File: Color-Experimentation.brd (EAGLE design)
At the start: 40.6 x 69.5 mm, 26 parts, among them J1 10118193-0001LF, U2 ATTINY85-20MUR

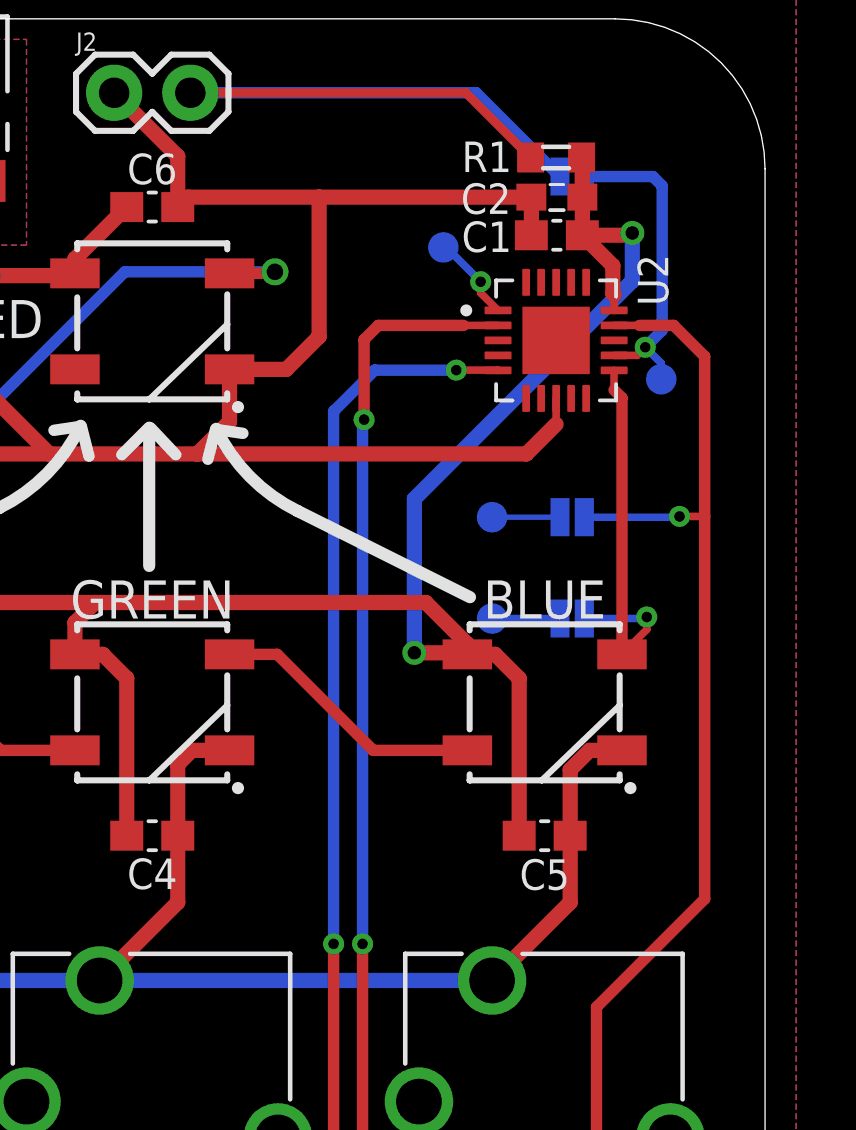
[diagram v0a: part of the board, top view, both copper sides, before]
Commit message: Switch microcontroller for availability: v1.1
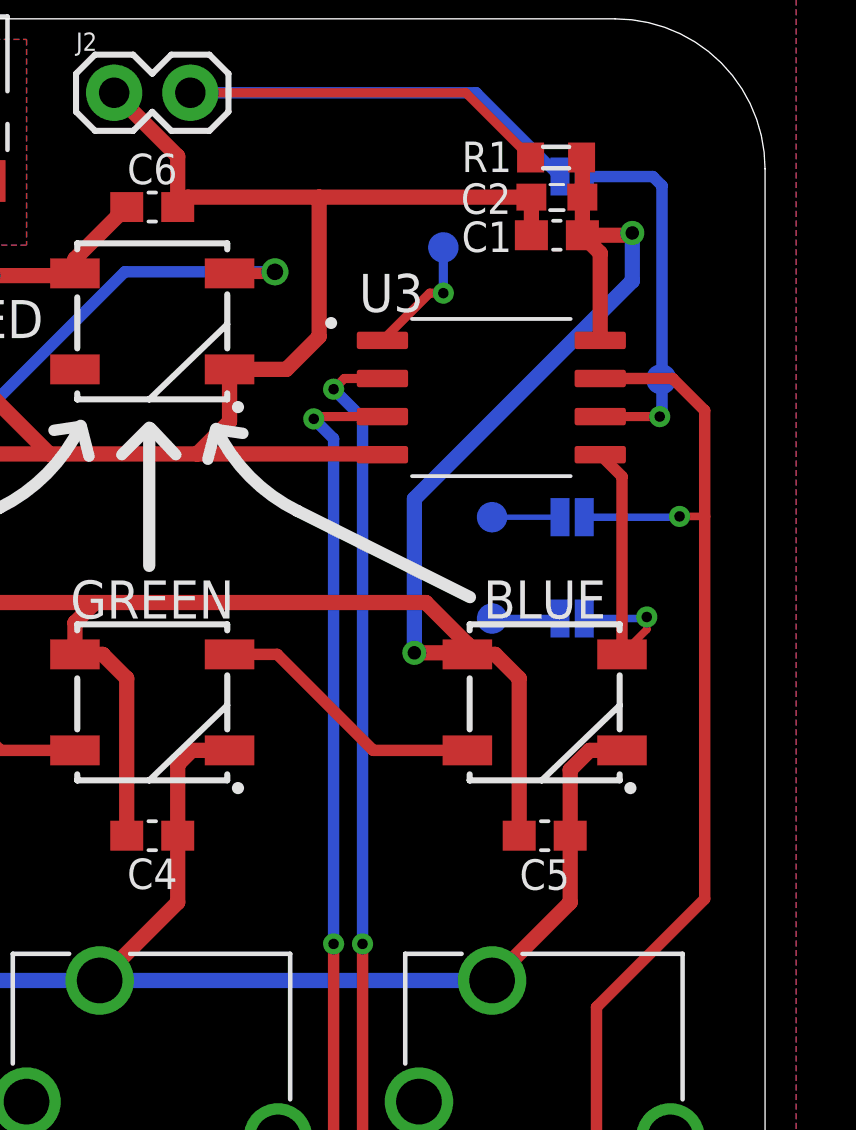
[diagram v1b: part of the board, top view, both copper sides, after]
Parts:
- removed U2: ATTINY85-20MUR, Color-Experimentation:QFN-20-THERMAL
- added U3: ATTINY85-20SU, Color-Experimentation:SOIC127P798X216-8N
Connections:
- net GND: now also U3.4; no longer U2.8
- net LED_DATA_OUT: now also U3.5; no longer U2.11
- net N$4: now also U3.1; no longer U2.1
- net N$6: now also U3.6; no longer U2.12
- net POT_BLUE_IN_A: now also U3.7; no longer U2.14
- net POT_GREEN_IN_A: now also U3.2; no longer U2.2
- net POT_RED_IN_A: now also U3.3; no longer U2.5
- net V_USB: now also U3.8; no longer U2.15
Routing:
- net GND: track 147.7 -> 140.7 mm
- net POT_GREEN_IN_A: track 63.1 -> 58.9 mm
- net POT_RED_IN_A: track 73.9 -> 70.2 mm
- net N$6: track 10.8 -> 13.7 mm
- net LED_DATA_OUT: track 13.3 -> 10.6 mm
- net N$4: track 2.91 -> 4.35 mm
- net POT_BLUE_IN_A: track 63.0 -> 61.7 mm
- net V_USB: track 175.9 -> 176.7 mm
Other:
- board text added: "Color Explorer v1.1"
- board text removed: "Color Explorer v1.0"

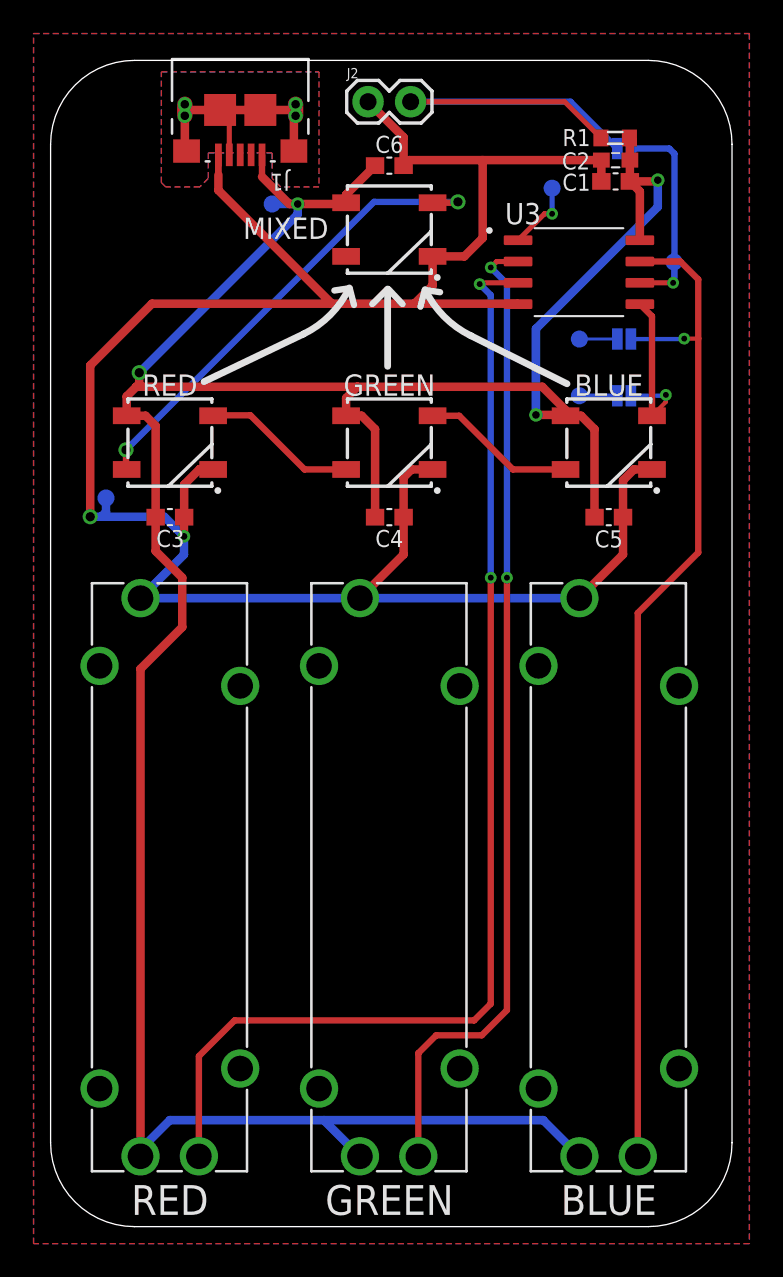
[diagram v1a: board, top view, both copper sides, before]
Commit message: Various improvements to address #2
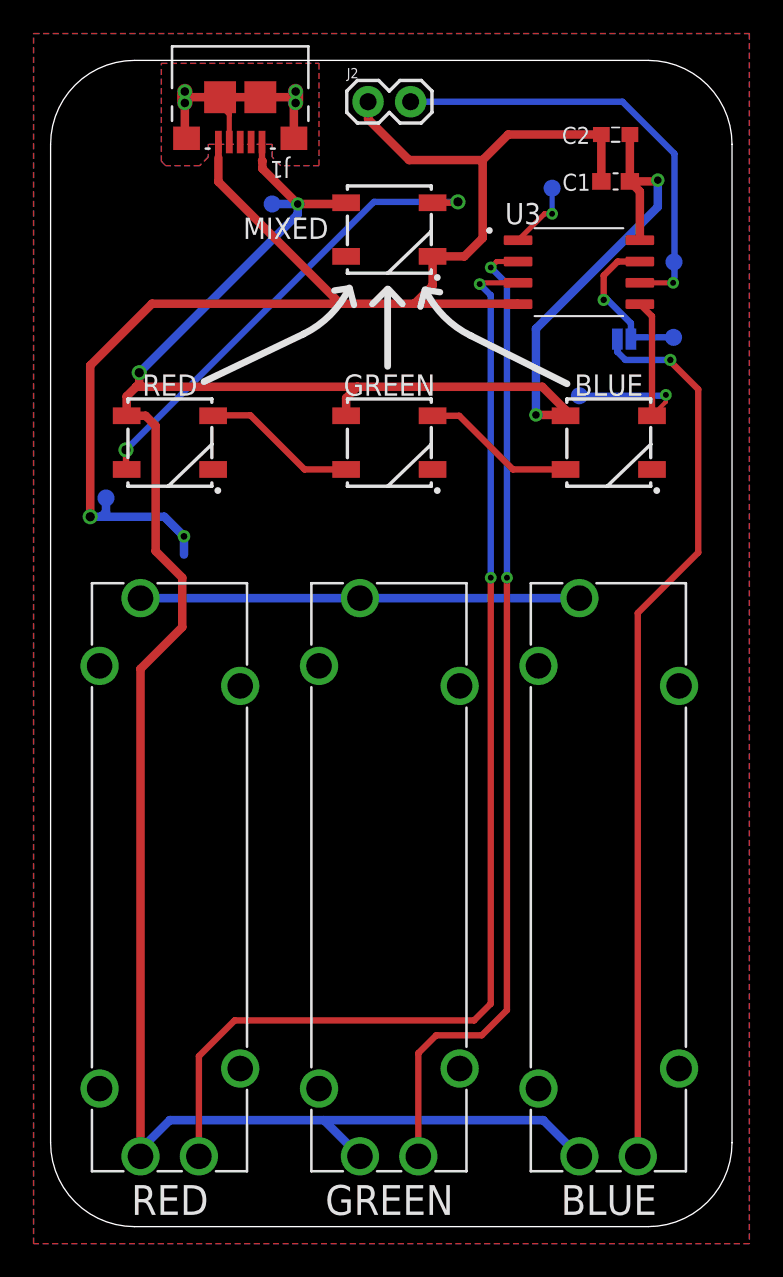
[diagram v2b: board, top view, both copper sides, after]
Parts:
- removed C3, C4, C5, C6: 0.1uF, Color-Experimentation:CAP_0603
- removed JP2, JP3: JUMPER-SMT_2_NO_SILK, Color-Experimentation:SMT-JUMPER_2_NO_SILK
- removed R1: 10k, Color-Experimentation:R0603
- moved SCK 5.61 mm to (37.1, 53.0), turned to 180 degrees
- moved C2 1.52 mm to (33.7, 65.1)
- moved J1 0.76 mm to (11.3, 67.3)
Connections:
- removed net MOSI: JP2.1, MOSI.P$1
- removed net N$3: J2.2, JP3.1, R1.2
- removed net SCK: JP1.2, SCK.P$1
- new net N$7: JP1.1, SCK.P$1, U3.7
- net GND: no longer C3.2, C4.2, C5.2, C6.2
- net LED_DATA_OUT: now also MOSI.P$1; no longer JP2.2
- net N$6: now also J2.2; no longer JP3.2
- net POT_BLUE_IN_A: now also JP1.2; no longer JP1.1, U3.7
- net V_USB: no longer C3.1, C4.1, C5.1, C6.1, R1.1
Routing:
- net GND: track 140.7 -> 114.0 mm
- net N$3: track 25.7 -> 0.00 mm
- net V_USB: track 176.7 -> 159.9 mm
- net N$6: track 13.7 -> 28.0 mm
- net N$7: track 0.00 -> 9.68 mm, vias 0 -> 1
- net POT_BLUE_IN_A: track 61.7 -> 53.8 mm
- net LED_DATA_OUT: track 10.6 -> 13.7 mm
- net SCK: track 2.26 -> 0.00 mm
- net MOSI: track 2.26 -> 0.00 mm
